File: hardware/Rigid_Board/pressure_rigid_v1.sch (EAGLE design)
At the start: 97 parts

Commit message: Wired up connectors
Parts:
- removed RPI_BUS: RASPBERRYPI-40-PIN-GPIO_PTH_NO_SHROUD, SparkFun-Connectors:RASPBERRYPI-40-PIN-GPIO_PTH_NO_SHROUD
- removed U$1: 64GRID, Pressure_Pad:64GRID
- added ANALOG_CONNECTOR, U$3: PCB_CONNECTOR_64_PIN, Pressure_Pad:PCB_CONNECTOR_64_PIN
- added M1: ARDUINO_R3_ICSP_NODIM, adafruit:ARDUINO_R3_ICSP_NODIM
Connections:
- new net N$66: C2.2, M1.GND@1
- new net N$67: C2.1, M1.3V
- new net P$100: DIGITAL_MUX3.GPA3, J5.8, U$3.P$36
- new net P$101: DIGITAL_MUX3.GPA4, J5.10, U$3.P$37
- new net P$102: DIGITAL_MUX3.GPA5, J5.12, U$3.P$38
- new net P$103: DIGITAL_MUX3.GPA6, J5.14, U$3.P$39
- new net P$104: DIGITAL_MUX3.GPA7, J5.16, U$3.P$40
- new net P$105: DIGITAL_MUX3.GPB0, J6.2, U$3.P$41
- new net P$106: DIGITAL_MUX3.GPB1, J6.4, U$3.P$42
- new net P$107: DIGITAL_MUX3.GPB2, J6.6, U$3.P$43
- new net P$108: DIGITAL_MUX3.GPB3, J6.8, U$3.P$44
- new net P$109: DIGITAL_MUX3.GPB4, J6.10, U$3.P$45
- new net P$110: DIGITAL_MUX3.GPB5, J6.12, U$3.P$46
- new net P$111: DIGITAL_MUX3.GPB6, J6.14, U$3.P$47
- new net P$112: DIGITAL_MUX3.GPB7, J6.16, U$3.P$48
- new net P$113: DIGITAL_MUX4.GPA0, J7.2, U$3.P$49
- new net P$114: DIGITAL_MUX4.GPA1, J7.4, U$3.P$50
- new net P$115: DIGITAL_MUX4.GPA2, J7.6, U$3.P$51
- new net P$116: DIGITAL_MUX4.GPA3, J7.8, U$3.P$52
- new net P$117: DIGITAL_MUX4.GPA4, J7.10, U$3.P$53
- new net P$118: DIGITAL_MUX4.GPA5, J7.12, U$3.P$54
- new net P$119: DIGITAL_MUX4.GPA6, J7.14, U$3.P$55
- new net P$120: DIGITAL_MUX4.GPA7, J7.16, U$3.P$56
- new net P$121: DIGITAL_MUX4.GPB0, J8.2, U$3.P$57
- new net P$122: DIGITAL_MUX4.GPB1, J8.4, U$3.P$58
- new net P$123: DIGITAL_MUX4.GPB2, J8.6, U$3.P$59
- new net P$124: DIGITAL_MUX4.GPB3, J8.8, U$3.P$60
- new net P$125: DIGITAL_MUX4.GPB4, J8.10, U$3.P$61
- new net P$126: DIGITAL_MUX4.GPB5, J8.12, U$3.P$62
- new net P$127: DIGITAL_MUX4.GPB6, J8.14, U$3.P$63
- new net P$128: DIGITAL_MUX4.GPB7, J8.16, U$3.P$64
- new net P$65: DIGITAL_MUX1.GPA0, J1.2, U$3.P$1
- new net P$66: DIGITAL_MUX1.GPA1, J1.4, U$3.P$2
- new net P$67: DIGITAL_MUX1.GPA2, J1.6, U$3.P$3
- new net P$68: DIGITAL_MUX1.GPA3, J1.8, U$3.P$4
- new net P$69: DIGITAL_MUX1.GPA4, J1.10, U$3.P$5
- new net P$70: DIGITAL_MUX1.GPA5, J1.12, U$3.P$6
- new net P$71: DIGITAL_MUX1.GPA6, J1.14, U$3.P$7
- new net P$72: DIGITAL_MUX1.GPA7, J1.16, U$3.P$8
- new net P$73: DIGITAL_MUX1.GPB0, J2.2, U$3.P$9
- new net P$74: DIGITAL_MUX1.GPB1, J2.4, U$3.P$10
- new net P$75: DIGITAL_MUX1.GPB2, J2.6, U$3.P$11
- new net P$76: DIGITAL_MUX1.GPB3, J2.8, U$3.P$12
- new net P$77: DIGITAL_MUX1.GPB4, J2.10, U$3.P$13
- new net P$78: DIGITAL_MUX1.GPB5, J2.12, U$3.P$14
- new net P$79: DIGITAL_MUX1.GPB6, J2.14, U$3.P$15
- new net P$80: DIGITAL_MUX1.GPB7, J2.16, U$3.P$16
- new net P$81: DIGITAL_MUX2.GPA0, J3.2, U$3.P$17
- new net P$82: DIGITAL_MUX2.GPA1, J3.4, U$3.P$18
- new net P$83: DIGITAL_MUX2.GPA2, J3.6, U$3.P$19
- new net P$84: DIGITAL_MUX2.GPA3, J3.8, U$3.P$20
- new net P$85: DIGITAL_MUX2.GPA4, J3.10, U$3.P$21
- new net P$86: DIGITAL_MUX2.GPA5, J3.12, U$3.P$22
- new net P$87: DIGITAL_MUX2.GPA6, J3.14, U$3.P$23
- new net P$88: DIGITAL_MUX2.GPA7, J3.16, U$3.P$24
- new net P$89: DIGITAL_MUX2.GPB0, J4.2, U$3.P$25
- new net P$90: DIGITAL_MUX2.GPB1, J4.4, U$3.P$26
- new net P$91: DIGITAL_MUX2.GPB2, J4.6, U$3.P$27
- new net P$92: DIGITAL_MUX2.GPB3, J4.8, U$3.P$28
- new net P$93: DIGITAL_MUX2.GPB4, J4.10, U$3.P$29
- new net P$94: DIGITAL_MUX2.GPB5, J4.12, U$3.P$30
- new net P$95: DIGITAL_MUX2.GPB6, J4.14, U$3.P$31
- new net P$96: DIGITAL_MUX2.GPB7, J4.16, U$3.P$32
- new net P$97: DIGITAL_MUX3.GPA0, J5.2, U$3.P$33
- new net P$98: DIGITAL_MUX3.GPA1, J5.4, U$3.P$34
- new net P$99: DIGITAL_MUX3.GPA2, J5.6, U$3.P$35
- net 3.3V0: no longer C2.1, RPI_BUS.3.3V@1, RPI_BUS.3.3V@17
- net CLK: now also M1.SCK; no longer RPI_BUS.SCLK
- net CS: now also M1.D6; no longer RPI_BUS.CE0
- net D0: now also M1.D2; no longer RPI_BUS.GP5
- net D1: now also M1.D3; no longer RPI_BUS.GP6
- net D2: now also M1.D4; no longer RPI_BUS.GP12
- net D3: now also M1.D5; no longer RPI_BUS.GP13
- net GND: no longer C2.2, RPI_BUS.GND@14, RPI_BUS.GND@20, RPI_BUS.GND@25, RPI_BUS.GND@30, RPI_BUS.GND@34, RPI_BUS.GND@39, RPI_BUS.GND@6, RPI_BUS.GND@9
- net I2C$SCL: now also M1.SCL; no longer RPI_BUS.SCL
- net I2C$SDA: now also M1.SDA; no longer RPI_BUS.SDA
- net MISO: now also M1.MISO; no longer RPI_BUS.MISO
- net MOSI: now also M1.MOSI; no longer RPI_BUS.MOSI
- net P$1: now also ANALOG_CONNECTOR.P$1, J1.1; no longer DIGITAL_MUX1.GPA0, U$1.P$1
- net P$10: now also ANALOG_CONNECTOR.P$10, J2.3; no longer DIGITAL_MUX1.GPB1, U$1.P$10
- net P$11: now also ANALOG_CONNECTOR.P$11, J2.5; no longer DIGITAL_MUX1.GPB2, U$1.P$11
- net P$12: now also ANALOG_CONNECTOR.P$12, J2.7; no longer DIGITAL_MUX1.GPB3, U$1.P$12
- net P$13: now also ANALOG_CONNECTOR.P$13, J2.9; no longer DIGITAL_MUX1.GPB4, U$1.P$13
- net P$14: now also ANALOG_CONNECTOR.P$14, J2.11; no longer DIGITAL_MUX1.GPB5, U$1.P$14
- net P$15: now also ANALOG_CONNECTOR.P$15, J2.13; no longer DIGITAL_MUX1.GPB6, U$1.P$15
- net P$16: now also ANALOG_CONNECTOR.P$16, J2.15; no longer DIGITAL_MUX1.GPB7, U$1.P$16
- net P$17: now also ANALOG_CONNECTOR.P$17, J3.1; no longer DIGITAL_MUX2.GPA0, U$1.P$17
- net P$18: now also ANALOG_CONNECTOR.P$18, J3.3; no longer DIGITAL_MUX2.GPA1, U$1.P$18
- net P$19: now also ANALOG_CONNECTOR.P$19, J3.5; no longer DIGITAL_MUX2.GPA2, U$1.P$19
- net P$2: now also ANALOG_CONNECTOR.P$2, J1.3; no longer DIGITAL_MUX1.GPA1, U$1.P$2
- net P$20: now also ANALOG_CONNECTOR.P$20, J3.7; no longer DIGITAL_MUX2.GPA3, U$1.P$20
- net P$21: now also ANALOG_CONNECTOR.P$21, J3.9; no longer DIGITAL_MUX2.GPA4, U$1.P$21
- net P$22: now also ANALOG_CONNECTOR.P$22, J3.11; no longer DIGITAL_MUX2.GPA5, U$1.P$22
- net P$23: now also ANALOG_CONNECTOR.P$23, J3.13; no longer DIGITAL_MUX2.GPA6, U$1.P$23
- net P$24: now also ANALOG_CONNECTOR.P$24, J3.15; no longer DIGITAL_MUX2.GPA7, U$1.P$24
- net P$25: now also ANALOG_CONNECTOR.P$25, J4.1; no longer DIGITAL_MUX2.GPB0, U$1.P$25
- net P$26: now also ANALOG_CONNECTOR.P$26, J4.3; no longer DIGITAL_MUX2.GPB1, U$1.P$26
- net P$27: now also ANALOG_CONNECTOR.P$27, J4.5; no longer DIGITAL_MUX2.GPB2, U$1.P$27
- net P$28: now also ANALOG_CONNECTOR.P$28, J4.7; no longer DIGITAL_MUX2.GPB3, U$1.P$28
- net P$29: now also ANALOG_CONNECTOR.P$29, J4.9; no longer DIGITAL_MUX2.GPB4, U$1.P$29
- net P$3: now also ANALOG_CONNECTOR.P$3, J1.5; no longer DIGITAL_MUX1.GPA2, U$1.P$3
- net P$30: now also ANALOG_CONNECTOR.P$30, J4.11; no longer DIGITAL_MUX2.GPB5, U$1.P$30
- net P$31: now also ANALOG_CONNECTOR.P$31, J4.13; no longer DIGITAL_MUX2.GPB6, U$1.P$31
- net P$32: now also ANALOG_CONNECTOR.P$32, J4.15; no longer DIGITAL_MUX2.GPB7, U$1.P$32
- net P$33: now also ANALOG_CONNECTOR.P$33, J5.1; no longer DIGITAL_MUX3.GPA0, U$1.P$33
- net P$34: now also ANALOG_CONNECTOR.P$34, J5.3; no longer DIGITAL_MUX3.GPA1, U$1.P$34
- net P$35: now also ANALOG_CONNECTOR.P$35, J5.5; no longer DIGITAL_MUX3.GPA2, U$1.P$35
- net P$36: now also ANALOG_CONNECTOR.P$36, J5.7; no longer DIGITAL_MUX3.GPA3, U$1.P$36
- net P$37: now also ANALOG_CONNECTOR.P$37, J5.9; no longer DIGITAL_MUX3.GPA4, U$1.P$37
- net P$38: now also ANALOG_CONNECTOR.P$38, J5.11; no longer DIGITAL_MUX3.GPA5, U$1.P$38
- net P$39: now also ANALOG_CONNECTOR.P$39, J5.13; no longer DIGITAL_MUX3.GPA6, U$1.P$39
- net P$4: now also ANALOG_CONNECTOR.P$4, J1.7; no longer DIGITAL_MUX1.GPA3, U$1.P$4
- net P$40: now also ANALOG_CONNECTOR.P$40, J5.15; no longer DIGITAL_MUX3.GPA7, U$1.P$40
- net P$41: now also ANALOG_CONNECTOR.P$41, J6.1; no longer DIGITAL_MUX3.GPB0, U$1.P$41
- net P$42: now also ANALOG_CONNECTOR.P$42, J6.3; no longer DIGITAL_MUX3.GPB1, U$1.P$42
- net P$43: now also ANALOG_CONNECTOR.P$43, J6.5; no longer DIGITAL_MUX3.GPB2, U$1.P$43
- net P$44: now also ANALOG_CONNECTOR.P$44, J6.7; no longer DIGITAL_MUX3.GPB3, U$1.P$44
- net P$45: now also ANALOG_CONNECTOR.P$45, J6.9; no longer DIGITAL_MUX3.GPB4, U$1.P$45
- net P$46: now also ANALOG_CONNECTOR.P$46, J6.11; no longer DIGITAL_MUX3.GPB5, U$1.P$46
- net P$47: now also ANALOG_CONNECTOR.P$47, J6.13; no longer DIGITAL_MUX3.GPB6, U$1.P$47
- net P$48: now also ANALOG_CONNECTOR.P$48, J6.15; no longer DIGITAL_MUX3.GPB7, U$1.P$48
- net P$49: now also ANALOG_CONNECTOR.P$49, J7.1; no longer DIGITAL_MUX4.GPA0, U$1.P$49
- net P$5: now also ANALOG_CONNECTOR.P$5, J1.9; no longer DIGITAL_MUX1.GPA4, U$1.P$5
- net P$50: now also ANALOG_CONNECTOR.P$50, J7.3; no longer DIGITAL_MUX4.GPA1, U$1.P$50
- net P$51: now also ANALOG_CONNECTOR.P$51, J7.5; no longer DIGITAL_MUX4.GPA2, U$1.P$51
- net P$52: now also ANALOG_CONNECTOR.P$52, J7.7; no longer DIGITAL_MUX4.GPA3, U$1.P$52
- net P$53: now also ANALOG_CONNECTOR.P$53, J7.9; no longer DIGITAL_MUX4.GPA4, U$1.P$53
- net P$54: now also ANALOG_CONNECTOR.P$54, J7.11; no longer DIGITAL_MUX4.GPA5, U$1.P$54
- net P$55: now also ANALOG_CONNECTOR.P$55, J7.13; no longer DIGITAL_MUX4.GPA6, U$1.P$55
- net P$56: now also ANALOG_CONNECTOR.P$56, J7.15; no longer DIGITAL_MUX4.GPA7, U$1.P$56
- net P$57: now also ANALOG_CONNECTOR.P$57, J8.1; no longer DIGITAL_MUX4.GPB0, U$1.P$57
- net P$58: now also ANALOG_CONNECTOR.P$58, J8.3; no longer DIGITAL_MUX4.GPB1, U$1.P$58
- net P$59: now also ANALOG_CONNECTOR.P$59, J8.5; no longer DIGITAL_MUX4.GPB2, U$1.P$59
- net P$6: now also ANALOG_CONNECTOR.P$6, J1.11; no longer DIGITAL_MUX1.GPA5, U$1.P$6
- net P$60: now also ANALOG_CONNECTOR.P$60, J8.7; no longer DIGITAL_MUX4.GPB3, U$1.P$60
- net P$61: now also ANALOG_CONNECTOR.P$61, J8.9; no longer DIGITAL_MUX4.GPB4, U$1.P$61
- net P$62: now also ANALOG_CONNECTOR.P$62, J8.11; no longer DIGITAL_MUX4.GPB5, U$1.P$62
- net P$63: now also ANALOG_CONNECTOR.P$63, J8.13; no longer DIGITAL_MUX4.GPB6, U$1.P$63
- net P$64: now also ANALOG_CONNECTOR.P$64, J8.15; no longer DIGITAL_MUX4.GPB7, U$1.P$64
- net P$7: now also ANALOG_CONNECTOR.P$7, J1.13; no longer DIGITAL_MUX1.GPA6, U$1.P$7
- net P$8: now also ANALOG_CONNECTOR.P$8, J1.15; no longer DIGITAL_MUX1.GPA7, U$1.P$8
- net P$9: now also ANALOG_CONNECTOR.P$9, J2.1; no longer DIGITAL_MUX1.GPB0, U$1.P$9
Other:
- moved on the sheet: C2, J1, J2, J3, J4, J5, J6, J7, J8

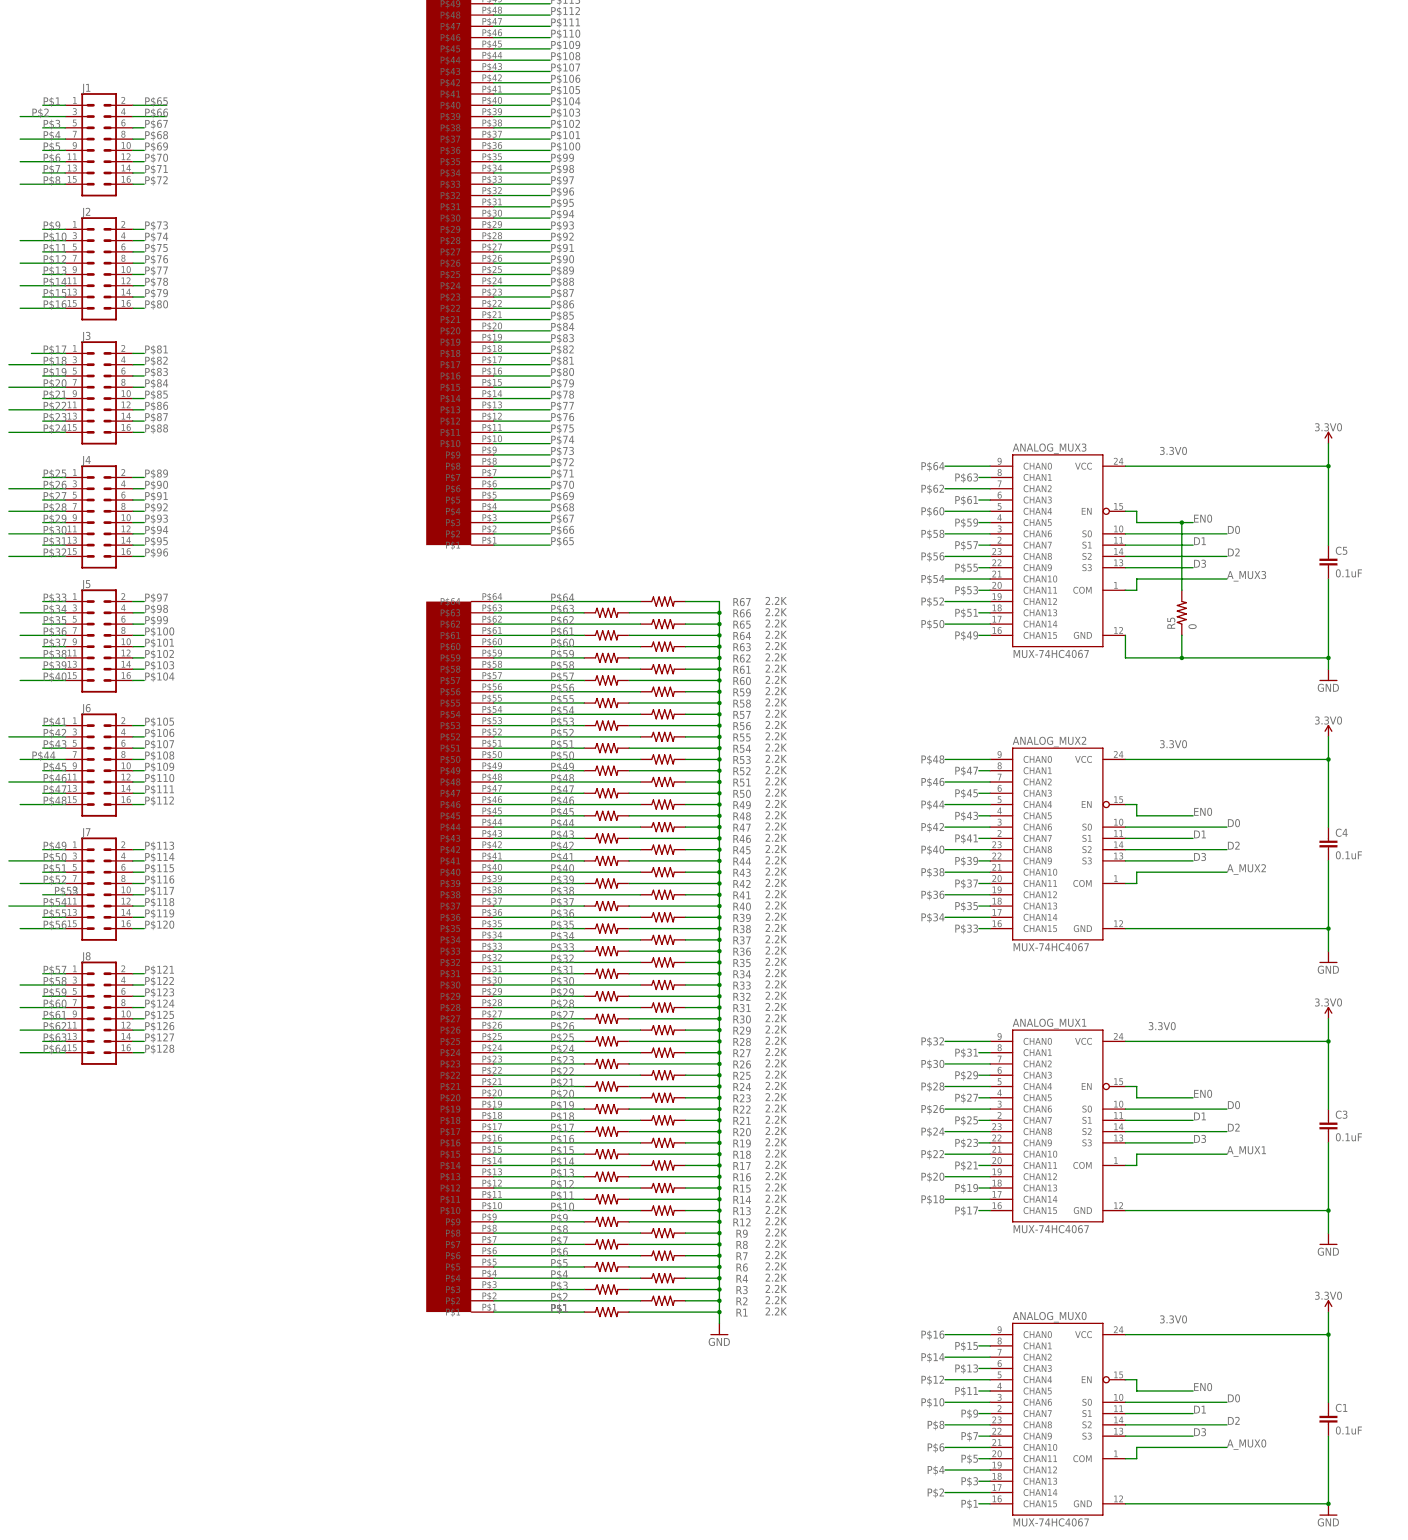
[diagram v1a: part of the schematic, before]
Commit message: Board redesign
Removed a ton of resistors, added SMD headers, and simplfied board.
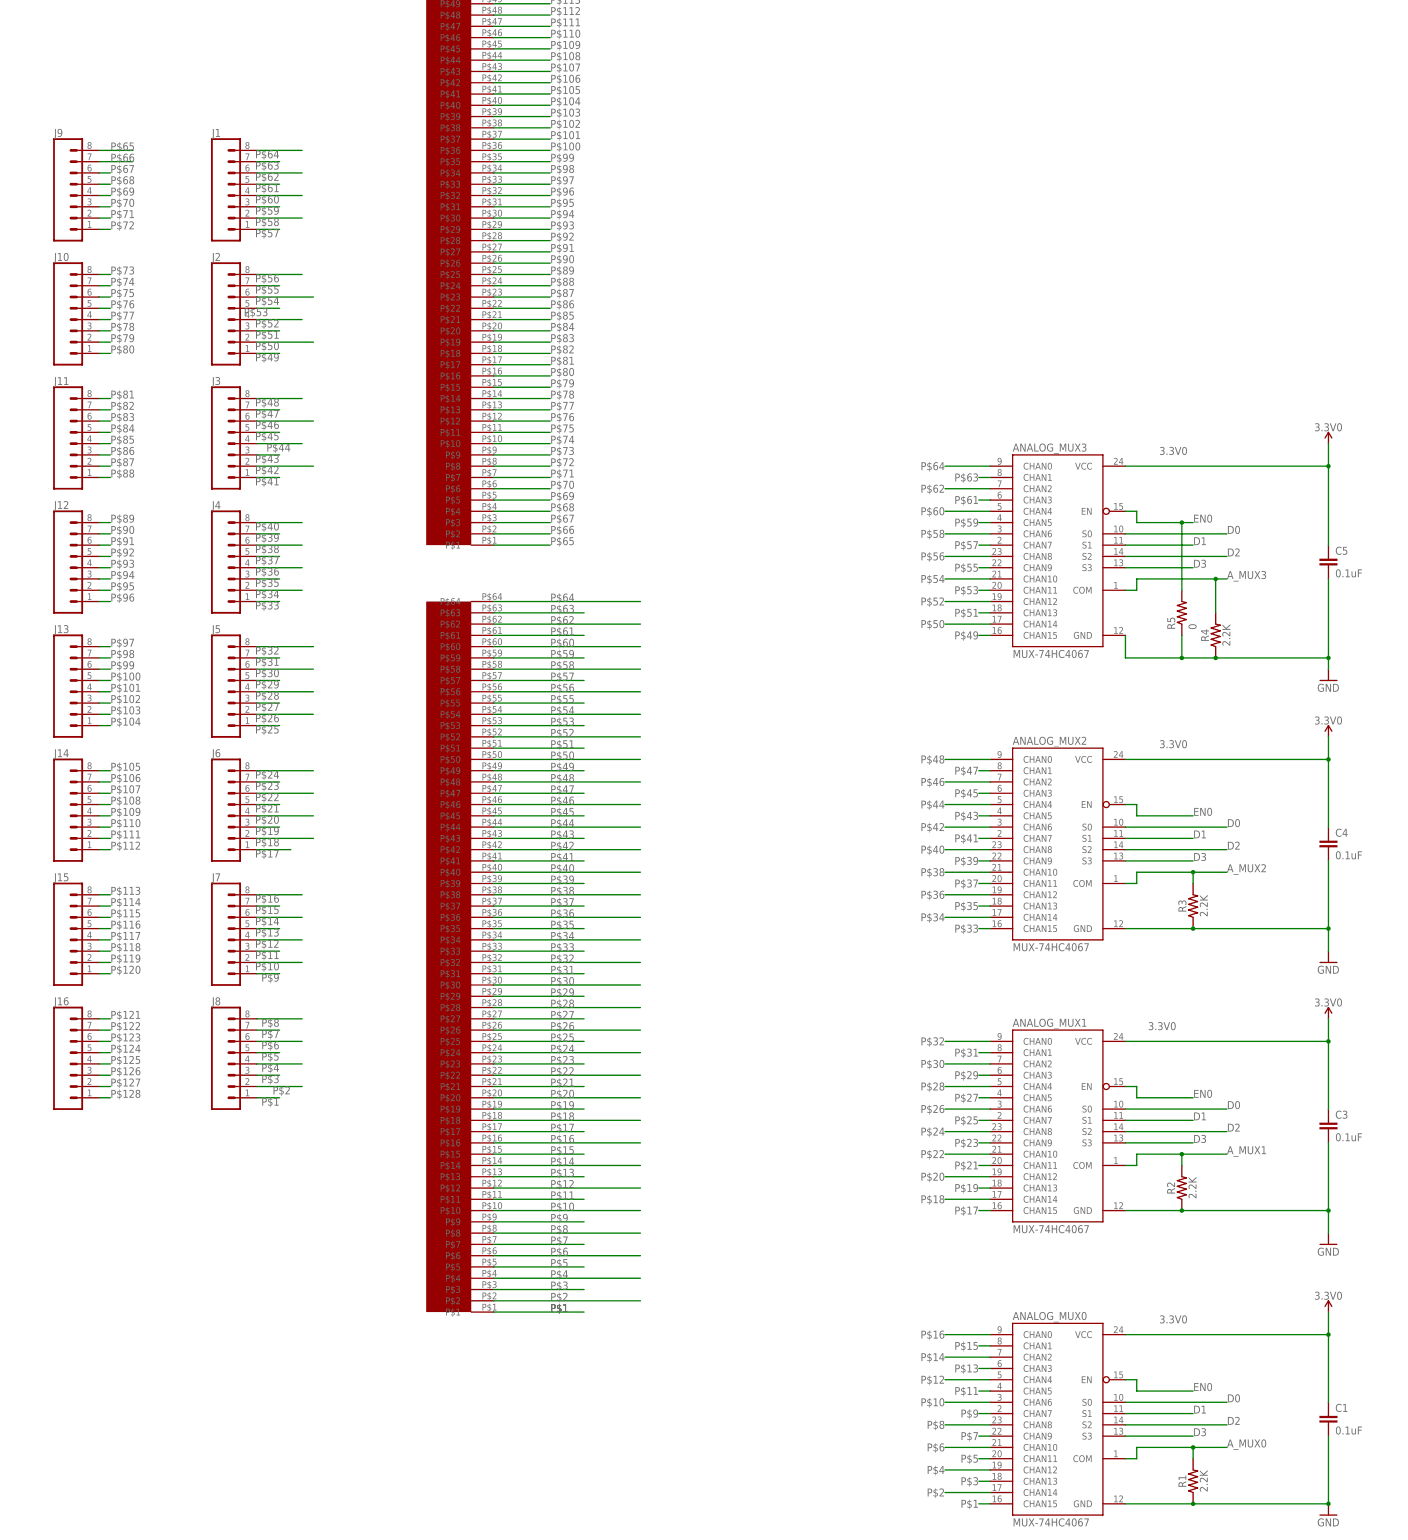
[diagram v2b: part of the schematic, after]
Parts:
- removed R12, R13, R14, R15, R16, R17, R18, R19, R20, R21, R22, R23, R24, R25, R26, R27, R28, R29, R30, R31, R32, R33, R34, R35, R36, R37, R38, R39, R40, R41, R42, R43, R44, R45, R46, R47, R48, R49, R50, R51, R52, R53, R54, R55, R56, R57, R58, R59, R6, R60, R61, R62, R63, R64, R65, R66, R67, R7, R8, R9: 2.2K, SparkFun-Resistors:100KOHM-0402-1/16W-1%
- added J10, J11, J12, J13, J14, J15, J16, J9: (no value), SparkFun-Connectors:CONN_08SMD-STRAIGHT-FEMALE
- J1, J2, J3, J4, J5, J6, J7, J8: device SparkFun-Connectors:CONN_08X2 -> SparkFun-Connectors:CONN_08SMD-STRAIGHT-FEMALE
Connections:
- net A_MUX0: now also R1.2
- net A_MUX1: now also R2.2
- net A_MUX2: now also R3.2
- net A_MUX3: now also R4.2
- net GND: now also R1.1, R2.1, R3.1, R4.1; no longer R1.2, R12.2, R13.2, R14.2, R15.2, R16.2, R17.2, R18.2, R19.2, R2.2, R20.2, R21.2, R22.2, R23.2, R24.2, R25.2, R26.2, R27.2, R28.2, R29.2, R3.2, R30.2, R31.2, R32.2, R33.2, R34.2, R35.2, R36.2, R37.2, R38.2, R39.2, R4.2, R40.2, R41.2, R42.2, R43.2, R44.2, R45.2, R46.2, R47.2, R48.2, R49.2, R50.2, R51.2, R52.2, R53.2, R54.2, R55.2, R56.2, R57.2, R58.2, R59.2, R6.2, R60.2, R61.2, R62.2, R63.2, R64.2, R65.2, R66.2, R67.2, R7.2, R8.2, R9.2
- net P$1: now also J8.1; no longer J1.1, R1.1
- net P$10: now also J7.2; no longer J2.3, R13.1
- net P$100: now also J13.5; no longer J5.8
- net P$101: now also J13.4; no longer J5.10
- net P$102: now also J13.3; no longer J5.12
- net P$103: now also J13.2; no longer J5.14
- net P$104: now also J13.1; no longer J5.16
- net P$105: now also J14.8; no longer J6.2
- net P$106: now also J14.7; no longer J6.4
- net P$107: now also J14.6; no longer J6.6
- net P$108: now also J14.5; no longer J6.8
- net P$109: now also J14.4; no longer J6.10
- net P$11: now also J7.3; no longer J2.5, R14.1
- net P$110: now also J14.3; no longer J6.12
- net P$111: now also J14.2; no longer J6.14
- net P$112: now also J14.1; no longer J6.16
- net P$113: now also J15.8; no longer J7.2
- net P$114: now also J15.7; no longer J7.4
- net P$115: now also J15.6; no longer J7.6
- net P$116: now also J15.5; no longer J7.8
- net P$117: now also J15.4; no longer J7.10
- net P$118: now also J15.3; no longer J7.12
- net P$119: now also J15.2; no longer J7.14
- net P$12: now also J7.4; no longer J2.7, R15.1
- net P$120: now also J15.1; no longer J7.16
- net P$121: now also J16.8; no longer J8.2
- net P$122: now also J16.7; no longer J8.4
- net P$123: now also J16.6; no longer J8.6
- net P$124: now also J16.5; no longer J8.8
- net P$125: now also J16.4; no longer J8.10
- net P$126: now also J16.3; no longer J8.12
- net P$127: now also J16.2; no longer J8.14
- net P$128: now also J16.1; no longer J8.16
- net P$13: now also J7.5; no longer J2.9, R16.1
- net P$14: now also J7.6; no longer J2.11, R17.1
- net P$15: now also J7.7; no longer J2.13, R18.1
- net P$16: now also J7.8; no longer J2.15, R19.1
- net P$17: now also J6.1; no longer J3.1, R20.1
- net P$18: now also J6.2; no longer J3.3, R21.1
- net P$19: now also J6.3; no longer J3.5, R22.1
- net P$2: now also J8.2; no longer J1.3, R2.1
- net P$20: now also J6.4; no longer J3.7, R23.1
- net P$21: now also J6.5; no longer J3.9, R24.1
- net P$22: now also J6.6; no longer J3.11, R25.1
- net P$23: now also J6.7; no longer J3.13, R26.1
- net P$24: now also J6.8; no longer J3.15, R27.1
- net P$25: now also J5.1; no longer J4.1, R28.1
- net P$26: now also J5.2; no longer J4.3, R29.1
- net P$27: now also J5.3; no longer J4.5, R30.1
- net P$28: now also J5.4; no longer J4.7, R31.1
- net P$29: now also J5.5; no longer J4.9, R32.1
- net P$3: now also J8.3; no longer J1.5, R3.1
- net P$30: now also J5.6; no longer J4.11, R33.1
- net P$31: now also J5.7; no longer J4.13, R34.1
- net P$32: now also J5.8; no longer J4.15, R35.1
- net P$33: now also J4.1; no longer J5.1, R36.1
- net P$34: now also J4.2; no longer J5.3, R37.1
- net P$35: now also J4.3; no longer J5.5, R38.1
- net P$36: now also J4.4; no longer J5.7, R39.1
- net P$37: now also J4.5; no longer J5.9, R40.1
- net P$38: now also J4.6; no longer J5.11, R41.1
- net P$39: now also J4.7; no longer J5.13, R42.1
- net P$4: now also J8.4; no longer J1.7, R4.1
- net P$40: now also J4.8; no longer J5.15, R43.1
- net P$41: now also J3.1; no longer J6.1, R44.1
- net P$42: now also J3.2; no longer J6.3, R45.1
- net P$43: now also J3.3; no longer J6.5, R46.1
- net P$44: now also J3.4; no longer J6.7, R47.1
- net P$45: now also J3.5; no longer J6.9, R48.1
- net P$46: now also J3.6; no longer J6.11, R49.1
- net P$47: now also J3.7; no longer J6.13, R50.1
- net P$48: now also J3.8; no longer J6.15, R51.1
- net P$49: now also J2.1; no longer J7.1, R52.1
- net P$5: now also J8.5; no longer J1.9, R6.1
- net P$50: now also J2.2; no longer J7.3, R53.1
- net P$51: now also J2.3; no longer J7.5, R54.1
- net P$52: now also J2.4; no longer J7.7, R55.1
- net P$53: now also J2.5; no longer J7.9, R56.1
- net P$54: now also J2.6; no longer J7.11, R57.1
- net P$55: now also J2.7; no longer J7.13, R58.1
- net P$56: now also J2.8; no longer J7.15, R59.1
- net P$57: now also J1.1; no longer J8.1, R60.1
- net P$58: now also J1.2; no longer J8.3, R61.1
- net P$59: now also J1.3; no longer J8.5, R62.1
- net P$6: now also J8.6; no longer J1.11, R7.1
- net P$60: now also J1.4; no longer J8.7, R63.1
- net P$61: now also J1.5; no longer J8.9, R64.1
- net P$62: now also J1.6; no longer J8.11, R65.1
- net P$63: now also J1.7; no longer J8.13, R66.1
- net P$64: now also J1.8; no longer J8.15, R67.1
- net P$65: now also J9.8; no longer J1.2
- net P$66: now also J9.7; no longer J1.4
- net P$67: now also J9.6; no longer J1.6
- net P$68: now also J9.5; no longer J1.8
- net P$69: now also J9.4; no longer J1.10
- net P$7: now also J8.7; no longer J1.13, R8.1
- net P$70: now also J9.3; no longer J1.12
- net P$71: now also J9.2; no longer J1.14
- net P$72: now also J9.1; no longer J1.16
- net P$73: now also J10.8; no longer J2.2
- net P$74: now also J10.7; no longer J2.4
- net P$75: now also J10.6; no longer J2.6
- net P$76: now also J10.5; no longer J2.8
- net P$77: now also J10.4; no longer J2.10
- net P$78: now also J10.3; no longer J2.12
- net P$79: now also J10.2; no longer J2.14
- net P$8: now also J8.8; no longer J1.15, R9.1
- net P$80: now also J10.1; no longer J2.16
- net P$81: now also J11.8; no longer J3.2
- net P$82: now also J11.7; no longer J3.4
- net P$83: now also J11.6; no longer J3.6
- net P$84: now also J11.5; no longer J3.8
- net P$85: now also J11.4; no longer J3.10
- net P$86: now also J11.3; no longer J3.12
- net P$87: now also J11.2; no longer J3.14
- net P$88: now also J11.1; no longer J3.16
- net P$89: now also J12.8; no longer J4.2
- net P$9: now also J7.1; no longer J2.1, R12.1
- net P$90: now also J12.7; no longer J4.4
- net P$91: now also J12.6; no longer J4.6
- net P$92: now also J12.5; no longer J4.8
- net P$93: now also J12.4; no longer J4.10
- net P$94: now also J12.3; no longer J4.12
- net P$95: now also J12.2; no longer J4.14
- net P$96: now also J12.1; no longer J4.16
- net P$97: now also J13.8; no longer J5.2
- net P$98: now also J13.7; no longer J5.4
- net P$99: now also J13.6; no longer J5.6
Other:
- moved on the sheet: R1, R2, R3, R4
